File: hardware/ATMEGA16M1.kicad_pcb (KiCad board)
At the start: 2 copper layers, 48.3 x 48.3 mm, 24 parts, among them CON1 BARREL_JACK, IC1 ATMEGA16M1-A, J1 HEADER_16, J2 HEADER_16, J3 FTDI, SW1 SW_PUSH, U1 NCP1117ST50T3G, X1 16MHz

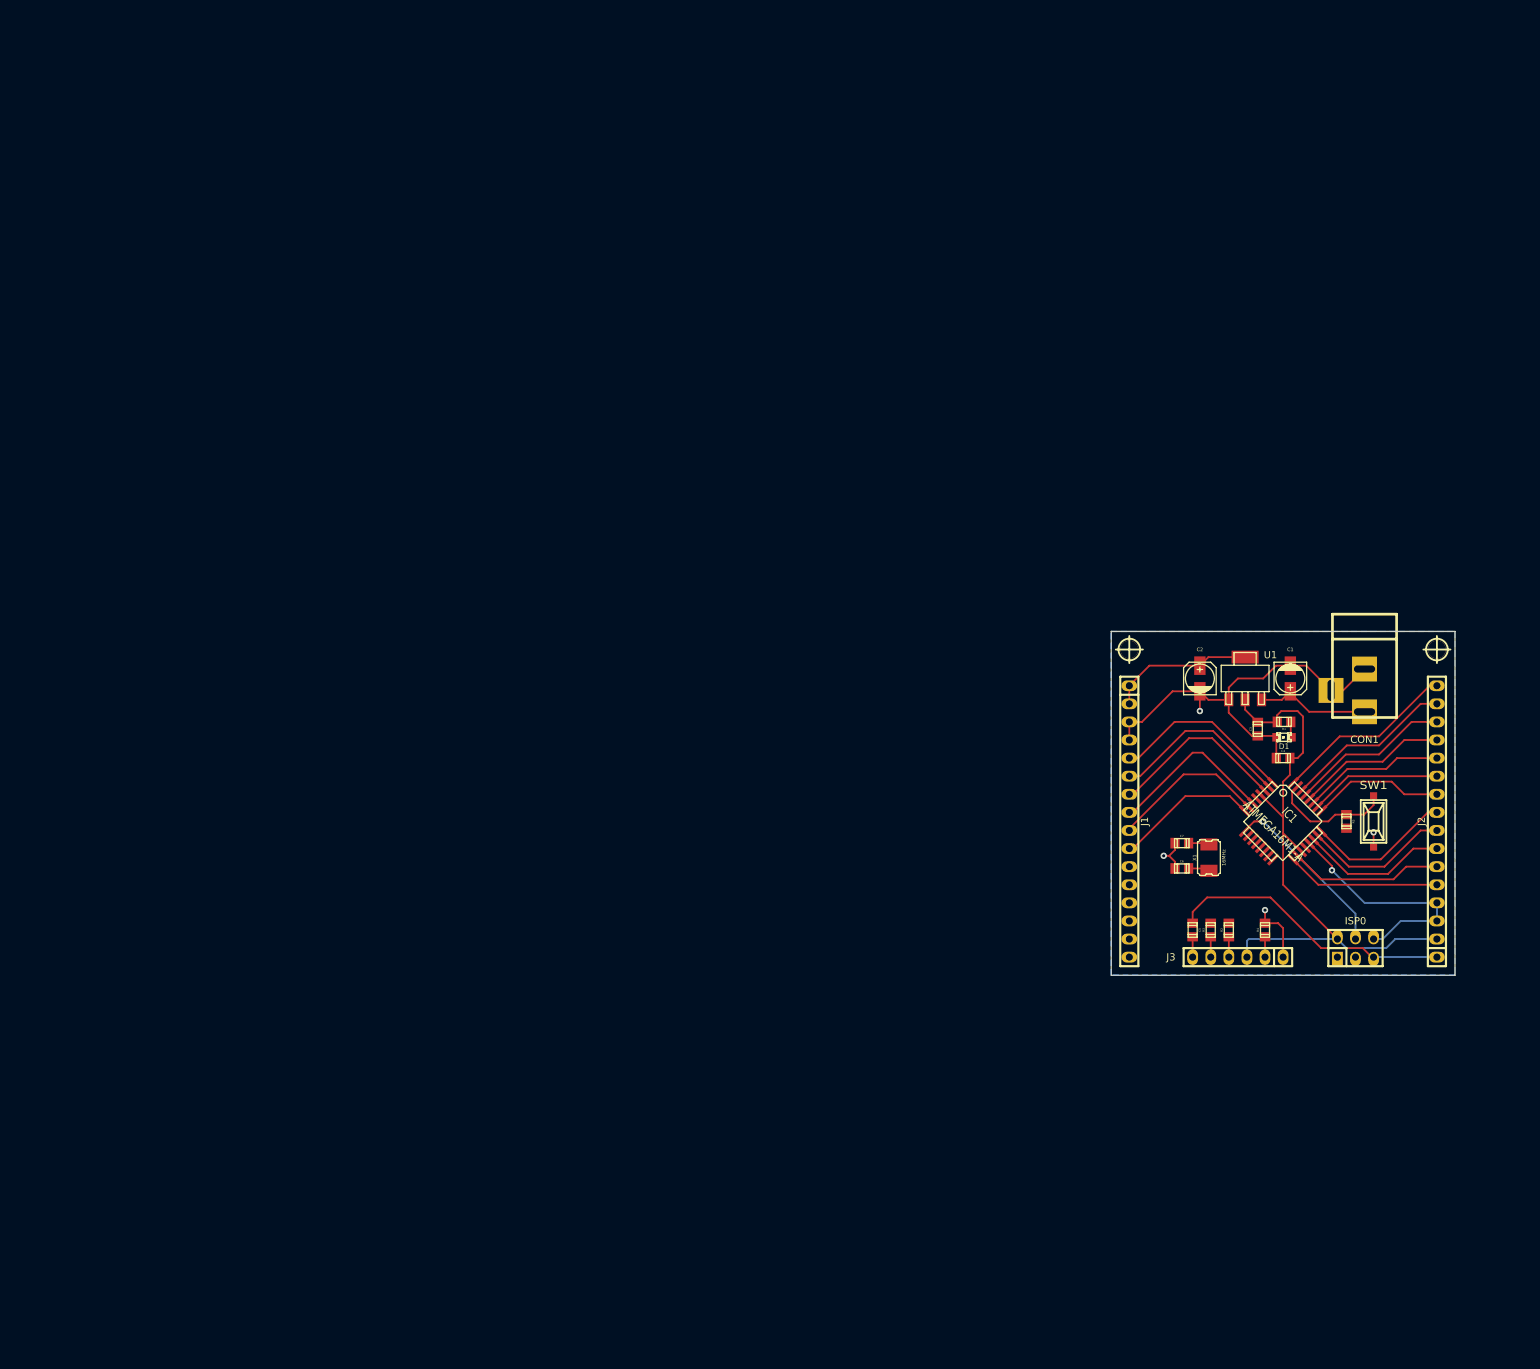
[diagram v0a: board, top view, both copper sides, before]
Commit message: PCB revisions: schematic update, cvpcb, pcb component grouping
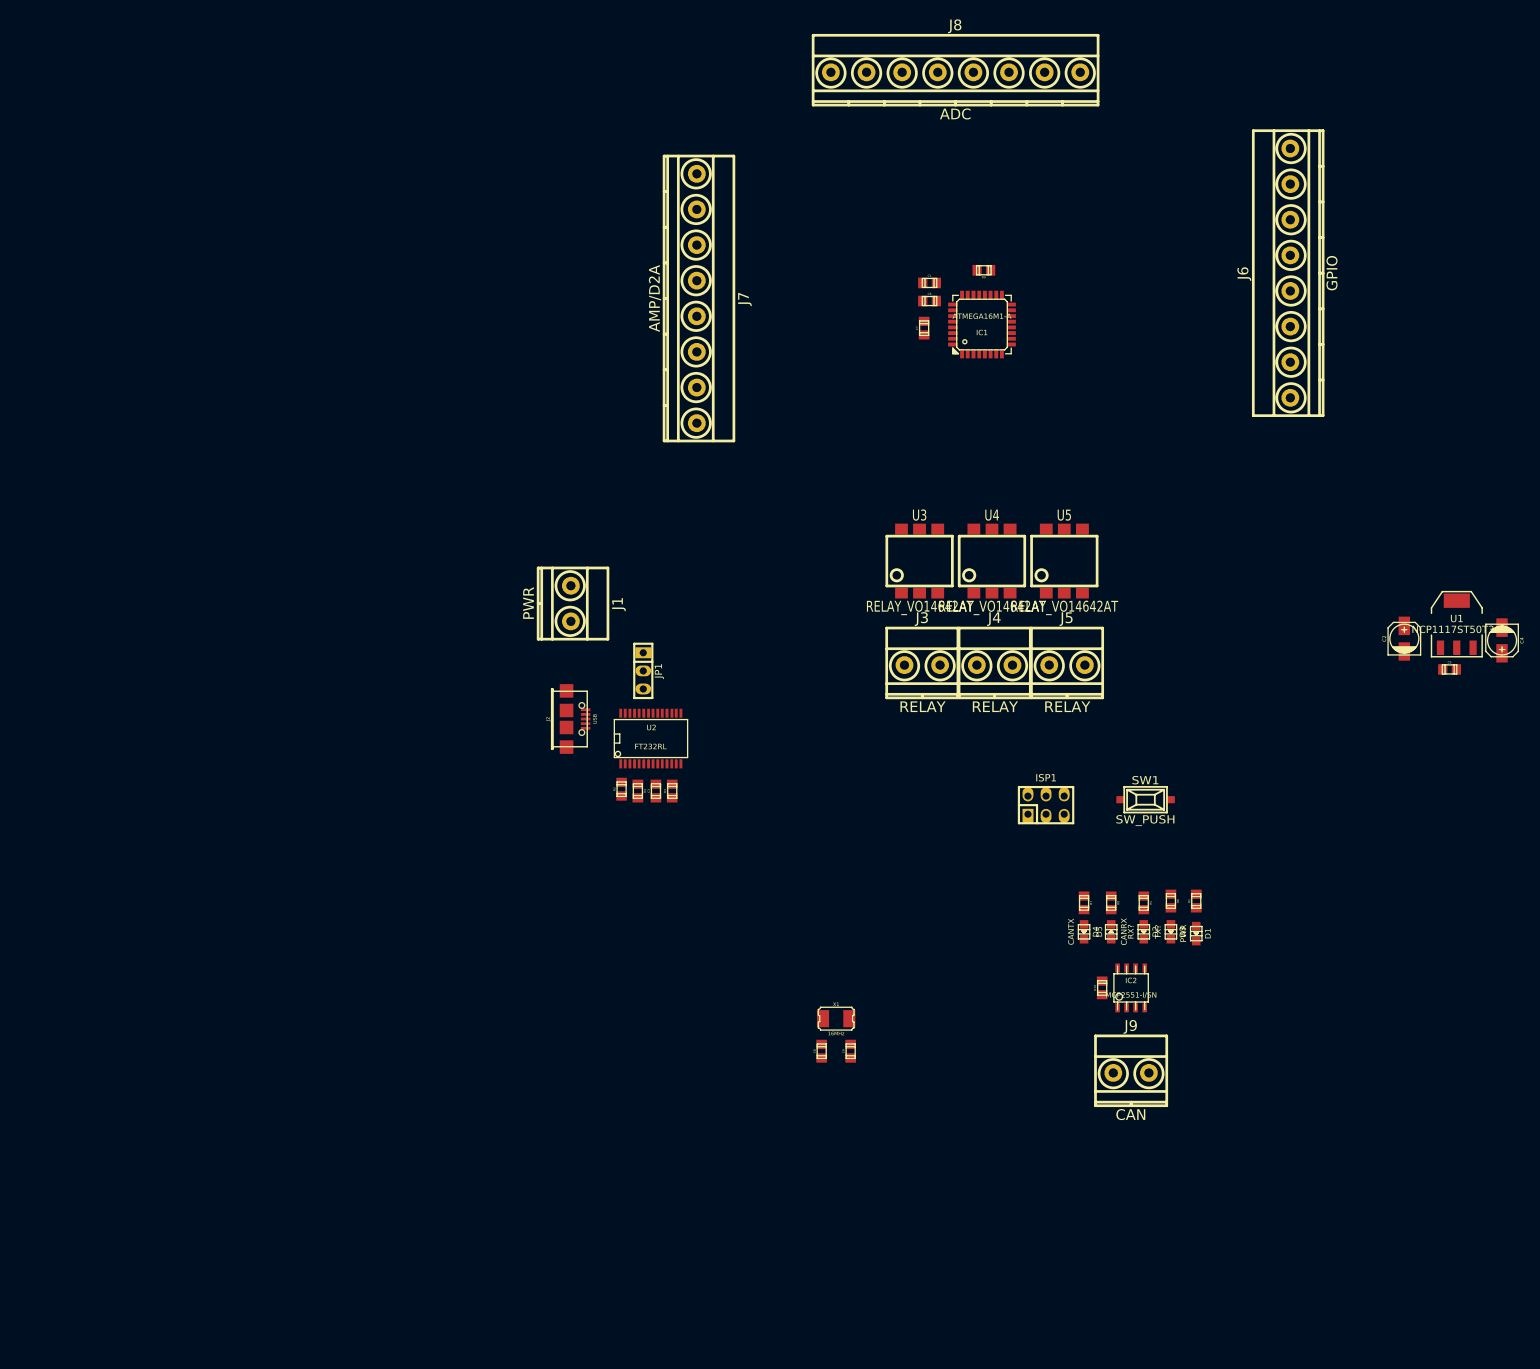
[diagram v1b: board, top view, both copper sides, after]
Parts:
- removed CON1: BARREL_JACK, BARREL_JACK
- removed ISP0: ISP0, pin_strip_3x2
- removed hole_2mm5 (x2): VAL**, hole_2mm5
- added C8: 22p, c_0805, F.Cu at (156.2, 178.3)
- added C9: 22p, c_0805, F.Cu at (160.3, 178.3)
- added D2: RX?, Led_0805, F.Cu at (201.4, 161.5)
- added D3: TX?, Led_0805, F.Cu at (205.2, 161.5)
- added D4: CANTX, Led_0805, F.Cu at (193.0, 161.5)
- added D5: CANRX, Led_0805, F.Cu at (196.8, 161.5)
- added IC2: MCP2551-I/SN, so-8, F.Cu at (199.6, 169.4)
- added ISP1: ISP1, pin_strip_3x2, F.Cu at (187.7, 143.8)
- added J4: RELAY, mkds_1,5-2, F.Cu at (180.5, 124.1)
- added J5: RELAY, mkds_1,5-2, F.Cu at (190.7, 124.1)
- added J6: GPIO, mkds_1,5-8, F.Cu at (222.0, 69.1)
- added J7: AMP/D2A, mkds_1,5-8, F.Cu at (138.7, 72.6)
- added J8: ADC, mkds_1,5-8, F.Cu at (175.0, 40.9)
- added J9: CAN, mkds_1,5-2, F.Cu at (199.6, 181.4)
- added JP1: JUMPER3, pin_strip_3, F.Cu at (131.2, 124.9)
- added R10: 10k, r_0805, F.Cu at (195.6, 169.4)
- added R6: 1k, r_0805, F.Cu at (205.2, 157.2)
- added R7: 1k, r_0805, F.Cu at (193.0, 157.5)
- added R8: 1k, r_0805, F.Cu at (196.8, 157.5)
- added R9: 10k, r_0805, F.Cu at (179.0, 68.7)
- added U2: FT232RL, SSOP28, F.Cu at (132.2, 134.4)
- added U3: RELAY_VO14642AT, mdip_6, F.Cu at (170.0, 109.5)
- added U4: RELAY_VO14642AT, mdip_6, F.Cu at (180.1, 109.5)
- added U5: RELAY_VO14642AT, mdip_6, F.Cu at (190.3, 109.5)
- C1: value 47u -> C; footprint c_elec_4x4.5 -> c_0805
- C2: footprint c_elec_4x4.5 -> c_elec_4x5.3
- C3: value 0.1 -> 0.1u
- C4: value 0.1u -> 47u; footprint c_0805 -> c_elec_4x5.3
- C5: value 0.1u -> 0.1
- C6, C7: value C -> 0.1u
- D1: value LED -> PWR; footprint LED-0805 -> Led_0805
- IC1: footprint TQFP32 -> lqfp32
- J1: value HEADER_16 -> PWR; footprint pin_socket_16 -> mkds_1,5-2
- J2: value HEADER_16 -> USB; footprint pin_socket_16 -> conn_usb_B_micro_smd-2
- J3: value FTDI -> RELAY; footprint pin_socket_6 -> mkds_1,5-2
- R5: value 10k -> 1k
- U1: footprint sot223 -> SOT223
- moved J2 123.0 mm to (120.4, 131.7), turned to 270 degrees
- moved R4 90.2 mm to (130.4, 141.8), turned to 270 degrees
- moved R2 87.5 mm to (128.1, 141.5)
- moved C6 87.2 mm to (171.3, 73.0)
- moved C3 84.9 mm to (132.9, 141.8)
- moved J1 84.1 mm to (121.0, 115.5)
- moved IC1 81.6 mm to (178.7, 76.3), turned to 0 degrees
- moved C7 80.8 mm to (170.6, 76.8), turned to 90 degrees
- moved R3 78.1 mm to (135.2, 141.8)
- moved C1 75.2 mm to (171.3, 70.5), turned to 0 degrees
- moved J3 60.4 mm to (170.3, 124.1), turned to 0 degrees
- moved X1 57.0 mm to (158.2, 173.7), turned to 0 degrees
- moved C5 51.4 mm to (244.3, 124.7), turned to 0 degrees
- moved C4 34.9 mm to (251.7, 120.7), turned to 270 degrees
- moved SW1 32.1 mm to (201.7, 143.0), turned to 0 degrees
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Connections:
- C1 pad 1: /V_IN -> VCC
- C2 pad 1: VCC -> /V_USER
- C3 pad 1: VCC -> /RTS
- C3 pad 2: GND -> /~RESET
- C5 pad 1: /RTS -> VCC
- C5 pad 2: /~RESET -> GND
- C6 pad 1: N-0000036 -> VCC
- C7 pad 1: N-0000035 -> /AREF
- IC1 pad 1: /PD2 -> /MISO_A
- IC1 pad 10: N-0000035 -> N-0000059
- IC1 pad 11: N-0000036 -> N-0000058
- IC1 pad 12: /PD4 -> /RXD
- IC1 pad 13: /PD5 -> /ADC2
- IC1 pad 14: /PD6 -> /ADC3
- IC1 pad 15: /PD7 -> /GPIO1
- IC1 pad 16: /PB2 -> /ADC5
- IC1 pad 17: /PC4 -> /AMP1-
- IC1 pad 18: /PC5 -> /AMP1+
- IC1 pad 2: /PD3 -> /MOSI_A
- IC1 pad 22: /PC6 -> /SSR0
- IC1 pad 23: /PB3 -> /AMP0-
- IC1 pad 24: /PB4 -> /AMP0+
- IC1 pad 25: /PC7 -> /D2A
- IC1 pad 26: /PB5 -> /GPIO0
- IC1 pad 27: /PB6 -> /ADC4
- IC1 pad 28: /PB7 -> /SCK
- IC1 pad 29: /PD0 -> /SSR1
- IC1 pad 3: /PC1 -> /PWM1
- IC1 pad 30: /PC0 -> /GPIO2
- IC1 pad 32: /PD1 -> /SSR2
- IC1 pad 6: /PC2 -> /CANTX
- IC1 pad 7: /PC3 -> /CANRX
- J1 pad 1: VCC -> /V_GLV
- J1 pad 2: VCC -> GND
- J2 pad 1: /~RESET -> /V_USB
- J2 pad 2: VCC -> /USBD-
- J2 pad 3: GND -> /USBD+
- J2 pad 4: /AREF -> GND
- J2 pad 5: /PC4 -> GND
- J3 pad 1: GND -> /SSR_0A
- J3 pad 2: /CTS -> /SSR_0B
- R2 pad 1: /PD4 -> /FTDI_TX
- R2 pad 2: /TXD -> /MOSI_A
- R3 pad 1: /PD3 -> /FTDI_RX
- R4 pad 2: /CTS -> /RTS
- R5 pad 1: VCC -> N-0000041
- R5 pad 2: /~RESET -> VCC
- U1 pad 3: /V_IN -> /V_USER
- X1 pad 1: N-0000036 -> N-0000058
- X1 pad 2: N-0000035 -> N-0000059
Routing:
- net VCC: track 106.7 -> 0.00 mm
- net GND: track 84.9 -> 0.00 mm, vias 4 -> 0
- net /~RESET: track 57.5 -> 0.00 mm
- net /PD2: track 25.8 -> 0.00 mm
- net /PD1: track 25.8 -> 0.00 mm
- net /PD3: track 25.5 -> 0.00 mm
- net /PC1: track 25.4 -> 0.00 mm
- net /MOSI: track 25.1 -> 0.00 mm, vias 1 -> 0
- net /AREF: track 24.4 -> 0.00 mm, vias 1 -> 0
- net /PC0: track 24.1 -> 0.00 mm
- net /PC2: track 23.8 -> 0.00 mm
- net /PD0: track 22.7 -> 0.00 mm
- net /PC3: track 22.1 -> 0.00 mm
- net /PC5: track 21.8 -> 0.00 mm
- net /PC4: track 21.7 -> 0.00 mm
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- removed copper zone on B.Cu, net GND
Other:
- board outline removed

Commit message: PCB rough initial layout
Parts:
- added R11: 220, r_0805, F.Cu at (81.3, 81.3)
- added R12: 220, r_0805, F.Cu at (99.1, 188.0)
- added R13: 220, r_0805, F.Cu at (114.3, 188.0)
- added hole_5mm: VAL**, hole_5mm, F.Cu at (61.0, 50.8)
- added hole_5mm: VAL**, hole_5mm, F.Cu at (61.0, 142.2)
- added hole_5mm: VAL**, hole_5mm, F.Cu at (152.4, 142.2)
- added hole_5mm: VAL**, hole_5mm, F.Cu at (152.4, 50.8)
- moved C2 162.6 mm to (75.4, 122.9)
- moved C4 162.6 mm to (89.2, 123.2)
- moved C5 162.6 mm to (81.8, 127.3)
- moved U1 162.6 mm to (82.8, 120.9)
- moved J4 122.5 mm to (96.5, 213.4)
- moved U4 121.8 mm to (96.5, 198.1), turned to 180 degrees
- moved J3 117.8 mm to (76.2, 53.3), turned to 180 degrees
- moved U3 103.3 mm to (76.2, 66.0)
- moved J5 88.7 mm to (137.2, 53.3), turned to 180 degrees
- moved ISP1 87.1 mm to (106.7, 111.8), turned to 180 degrees
- moved R10 83.8 mm to (121.9, 129.5)
- moved J9 83.7 mm to (127.0, 139.7)
- moved IC2 82.9 mm to (127.0, 129.5)
- moved J7 78.9 mm to (63.5, 96.5)
- moved J6 77.2 mm to (149.9, 96.5)
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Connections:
- J7 pad 8: (no net) -> GND
- U3 pad 1: /SSR0 -> N-0000036
- U4 pad 1: /SSR1 -> N-0000039
- U5 pad 1: /SSR2 -> N-0000038
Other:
- board outline added: 101.6 x 101.6 mm
- board text added: "ADC1"
- board text added: "ADC2"
- board text added: "ADC3"
- board text added: "ADC4"
- board text added: "ADC5"
- board text added: "AMP0+"
- board text added: "AMP0-"
- board text added: "AMP1+"
- board text added: "AMP1-"
- board text added: "AREF"
- board text added: "D2A"
- board text added: "GND"
- board text added: "GPIO0"
- board text added: "GPIO1"
- board text added: "GPIO2"
- board text added: "MISO"
- board text added: "MOSI"
- board text added: "PWM0"
- board text added: "PWM1"
- board text added: "SCK"
- board text added: "VCC"
